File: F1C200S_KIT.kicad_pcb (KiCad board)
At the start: 2 copper layers, 52 x 32.5 mm, 89 parts, among them J1 10.0402_LCD_RGB_CON_WJQ, J2 10.0002_USB_Micro, J3 10.0001_Micro_SD_Card, J4 10.0201_PH2X15_2D54_V, J5 10.0002_USB_Micro, J6 10.0202_PH2X9_2D54_V, SW1 11.0101_SW-A03-08, U1 08.0001_F1C200S, U2 09.0103_XC6206, U3 09.0102_EA3036, U4 09.0001_CP2104, U5 09.0303_GD5F1GQ4, U6 09.0302_W25Q128JVS, Y1 07.0403_Crystal_24M_3225

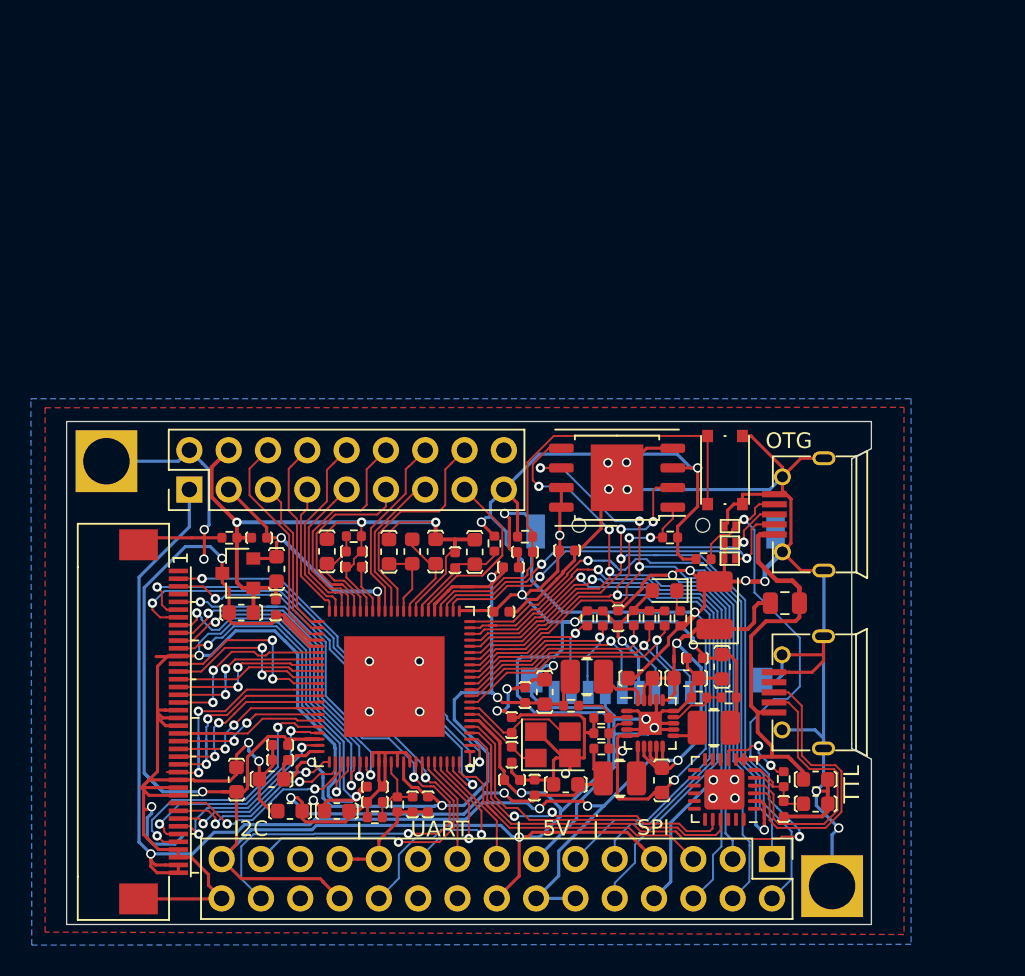
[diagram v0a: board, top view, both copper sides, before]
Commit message: Removed TV. Added USB. Refactored.
Signed-off-by: Sebastian Basierski <sebastian@basierski.pl>
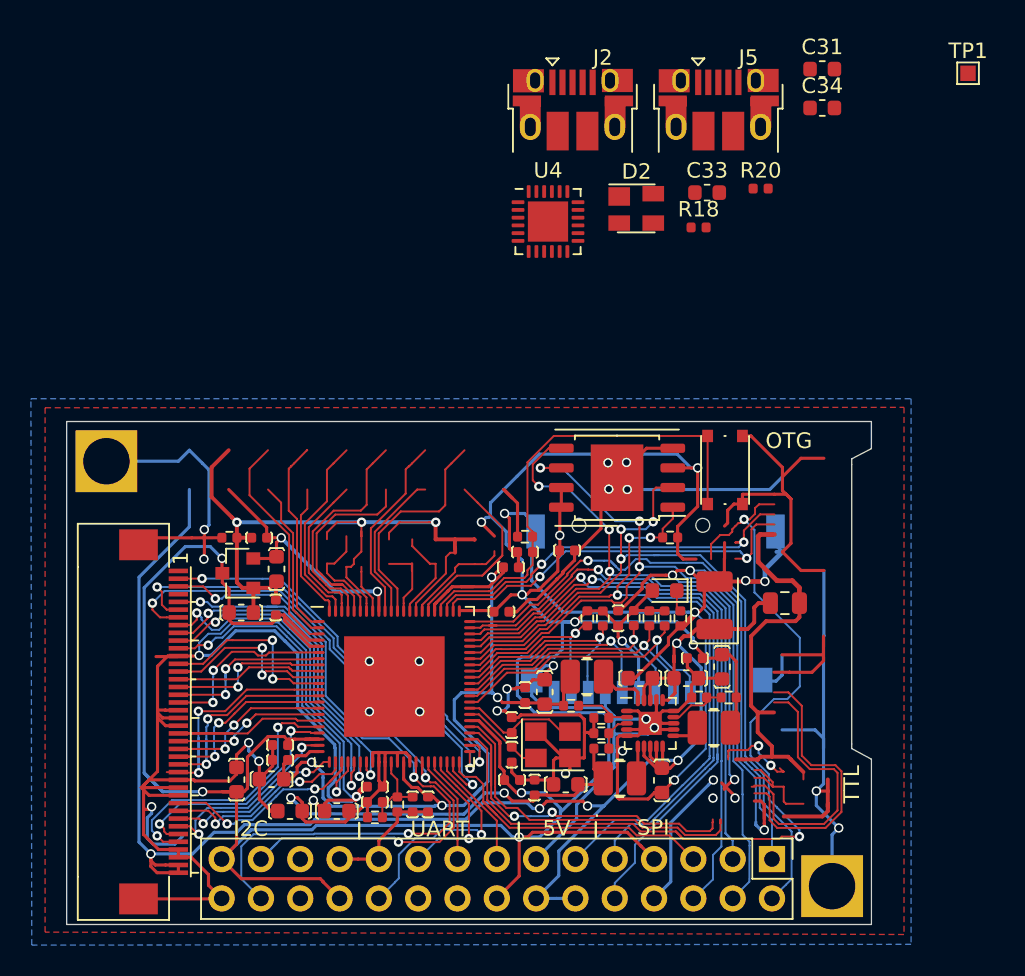
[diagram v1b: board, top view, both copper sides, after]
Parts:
- removed C38: 03.0001_C0402_1uF, 0WJQ:C_0402_WJQ
- removed C39, C43, C45: 03.4003_C0603_4.7uF, 0WJQ:C_0603_WJQ
- removed C40, C42: 03.0009_C0402_100nF, 0WJQ:C_0402_WJQ
- removed C41: 03.4004_C0603_10uF, 0WJQ:C_0603_WJQ
- removed C44: 03.0016_C0603_10uF, Capacitor_SMD:C_0603_1608Metric
- removed D3, D4, D5: 07.0002_D_TVS_PESDNC2FD5VB, 0WJQ:DFN1006-2L
- removed J6: 10.0202_PH2X9_2D54_V, Connector_PinHeader_2.54mm:PinHeader_2x09_P2.54mm_Vertical
- removed R21: 02.0027_R0402_200K_1%, 0WJQ:R_0402_WJQ
- removed R22: 02.0001_R0402_0R_1%, 0WJQ:R_0402_WJQ
- added D2: SP0503BAHT, Package_TO_SOT_SMD:SOT-143, F.Cu at (176.8, 86.2)
- added TP1: TestPoint, TestPoint:TestPoint_Pad_1.0x1.0mm, F.Cu at (198.2, 77.5)
- C31, C33: footprint 0WJQ:C_0603_WJQ -> Capacitor_SMD:C_0603_1608Metric
- C34: footprint 0WJQ:C_0402_WJQ -> Capacitor_SMD:C_0603_1608Metric
- J2, J5: footprint 0WJQ:MicroUSB_5S_B_A01SB141B1-067 -> Connector_USB:USB_Micro-B_Amphenol_10103594-0001LF_Horizontal
- R18, R20: footprint 0WJQ:R_0402_WJQ -> Resistor_SMD:R_0402_1005Metric
- moved C31 45.9 mm to (188.8, 77.2), turned to 0 degrees
- moved C34 45.4 mm to (188.8, 79.7), turned to 0 degrees
- moved J2 40.5 mm to (172.7, 79.8), turned to 0 degrees
- moved C33 40.1 mm to (181.4, 85.2), turned to 0 degrees
- moved U4 38.4 mm to (171.1, 87.1), turned to 0 degrees
- moved R18 36.1 mm to (180.8, 87.5), turned to 0 degrees
- moved J5 26.7 mm to (182.1, 79.8), turned to 0 degrees
- moved R20 24.2 mm to (184.8, 84.9)
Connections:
- net /CPU/CPU_RXD renamed /CPU_RXD
- net /CPU/CPU_TXD renamed /CPU_TXD
- net /CPU/PA0_UART1_RTS_SPI1_CS renamed /PA0_UART1_RTS_SPI1_CS
- net /CPU/PA1_UART1_CTS_SPI1_MOSI renamed /PA1_UART1_CTS_SPI1_MOSI
- net /CPU/PA2_UART1_RX_SPI1_CLK renamed /PA2_UART1_RX_SPI1_CLK
- net /CPU/PA3_UART1_TX_SPI1_MISO renamed /PA3_UART1_TX_SPI1_MISO
- net /CPU/PE10_UART2_CTS_SPI1_MISO renamed /PE10_UART2_CTS_SPI1_MISO
- net /CPU/PE11_TWI0_SCK renamed /PE11_TWI0_SCK
- net /CPU/PE12_TWI0_SDA renamed /PE12_TWI0_SDA
- net /CPU/PE5 renamed /PE5
- net /CPU/PE7_UART2_TX_SPI1_CS renamed /PE7_UART2_TX_SPI1_CS
- net /CPU/PE8_UART2_RX_SPI1_MOSI renamed /PE8_UART2_RX_SPI1_MOSI
- net /CPU/PE9_UART2_RTS_SPI1_CLK renamed /PE9_UART2_RTS_SPI1_CLK
- net /CPU/SDIO_CLK renamed /SDIO_CLK
- net /CPU/SDIO_CMD renamed /SDIO_CMD
- net /CPU/SDIO_D0 renamed /SDIO_D0
- net /CPU/SDIO_D1 renamed /SDIO_D1
- net /CPU/SDIO_D2 renamed /SDIO_D2
- net /CPU/SDIO_D3 renamed /SDIO_D3
- net /CPU/SPI0_CLK renamed /SPI0_CLK
- net /CPU/SPI0_CS renamed /SPI0_CS
- net /CPU/SPI0_MISO renamed /SPI0_MISO
- net /CPU/SPI0_MOSI renamed /SPI0_MOSI
- net /CPU/USB_D+ renamed /USB_D+
- net /CPU/USB_D- renamed /USB_D-
- net /CPU/USB_ID renamed /USB_ID
- net /Misc/CP2104_RST renamed /usb/CP2104_RST
- net /Misc/VBUS renamed /VBUS
- U1 pad 1: /CPU/HP_L -> (no net)
- U1 pad 2: /CPU/HP_COMFB -> (no net)
- U1 pad 3: /CPU/HP_COM -> (no net)
- U1 pad 72: /CPU/TV_OUT -> (no net)
- U1 pad 73: /CPU/TV_VCC -> Net-(TP1-Pad1)
- U1 pad 75: /CPU/TV_VRN -> (no net)
- U1 pad 76: /CPU/TV_VRP -> (no net)
- U1 pad 77: /CPU/TV_IN1 -> (no net)
- U1 pad 78: /CPU/TV_IN0 -> (no net)
- U1 pad 79: /CPU/LRADC0 -> (no net)
- U1 pad 81: /CPU/VRA1 -> (no net)
- U1 pad 83: /CPU/VRA2 -> (no net)
- U1 pad 84: /CPU/FMINL -> (no net)
- U1 pad 85: /CPU/FMINR -> (no net)
- U1 pad 86: /CPU/LINL -> (no net)
- U1 pad 87: /CPU/MICIN -> (no net)
- U1 pad 88: /CPU/HP_R -> (no net)
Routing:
- net Net-(U1-Pad85): track 0.00 -> 14.7 mm
- net /CPU/FMINR: track 14.7 -> 0.00 mm
- net Net-(U1-Pad77): track 0.00 -> 14.6 mm
- net /CPU/TV_IN1: track 14.6 -> 0.00 mm
- net Net-(U1-Pad84): track 0.00 -> 13.5 mm
- net /CPU/FMINL: track 13.5 -> 0.00 mm
- net Net-(U1-Pad72): track 0.00 -> 13.5 mm
- net /CPU/TV_OUT: track 13.5 -> 0.00 mm
- net Net-(U1-Pad87): track 0.00 -> 12.5 mm
- net /CPU/MICIN: track 12.5 -> 0.00 mm
- net Net-(U1-Pad79): track 0.00 -> 12.3 mm
- net /CPU/LRADC0: track 12.3 -> 0.00 mm
- net Net-(U1-Pad86): track 0.00 -> 10.4 mm
- net /CPU/LINL: track 10.4 -> 0.00 mm
- net Net-(U1-Pad78): track 0.00 -> 9.95 mm
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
